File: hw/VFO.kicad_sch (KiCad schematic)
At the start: 0 parts

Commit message: Starting design of RF front end and demod
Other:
- title: USB SSB Transciever overview -> VF)
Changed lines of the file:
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@@
 	(paper "A")
 	(title_block
-		(title "USB SSB Transciever overview")
+		(title "VF)")
 		(date "2025-03-23")
 		(company "SoftShack")

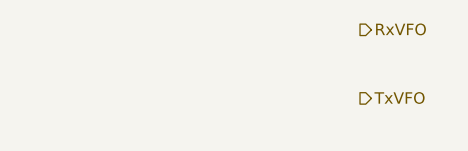
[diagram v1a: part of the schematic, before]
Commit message: Rx path is getting closer. Differential LO outputs from VFO. Clean up.
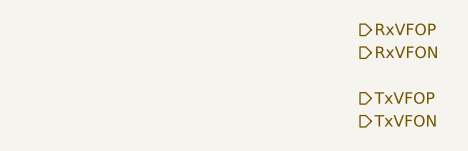
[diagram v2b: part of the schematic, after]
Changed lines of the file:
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@@
 		(comment 2 "WB7NAB")
 	)
-	(hierarchical_label "RxVFO"
+	(hierarchical_label "RxVFOP"
 		(shape output)
 		(at 256.54 25.4 0)
@@
 		)
 	)
-	(hierarchical_label "TxVFO"
+	(hierarchical_label "TxVFON"
+		(shape output)
+		(at 256.54 35.56 0)
+		(effects
+			(font
+				(size 1.27 1.27)
+			)
+			(justify left)
+		)
+	)
+	(hierarchical_label "TxVFOP"
 		(shape output)
 		(at 256.54 33.02 0)
@@
 		(effects
 			(font
+				(size 1.27 1.27)
+			)
+			(justify left)
+		)
+	)
+	(hierarchical_label "RxVFON"
+		(shape output)
+		(at 256.54 27.94 0)
+		(effects
+			(font

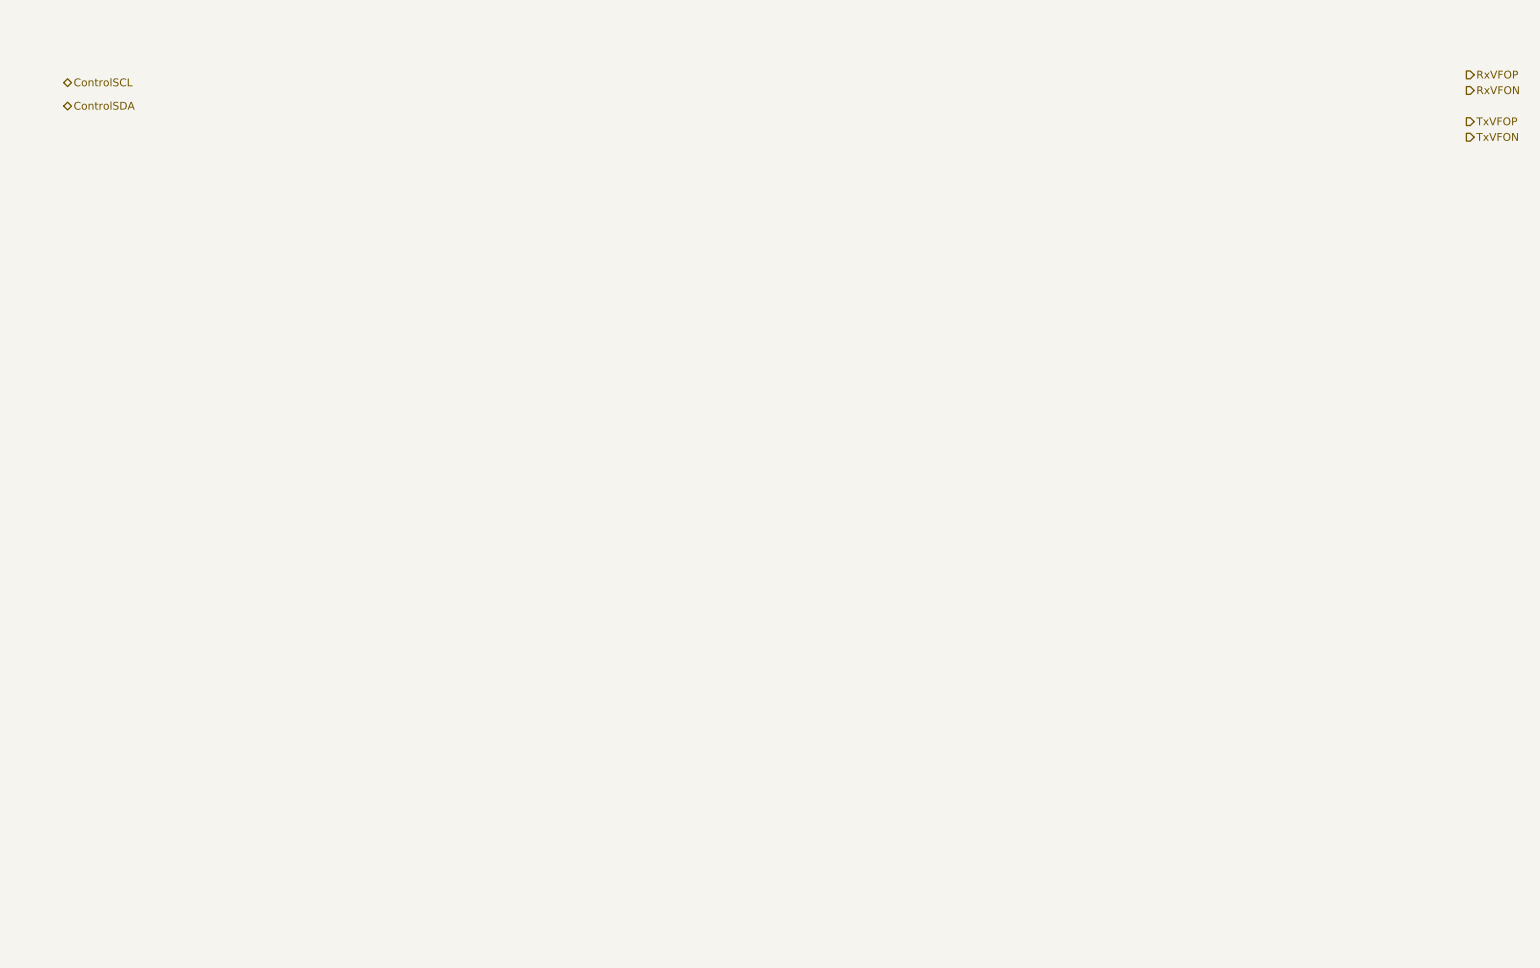
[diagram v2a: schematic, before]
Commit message: Checkpoint. More of rx path done. VFOs are now LVDS. Starting USB and power.
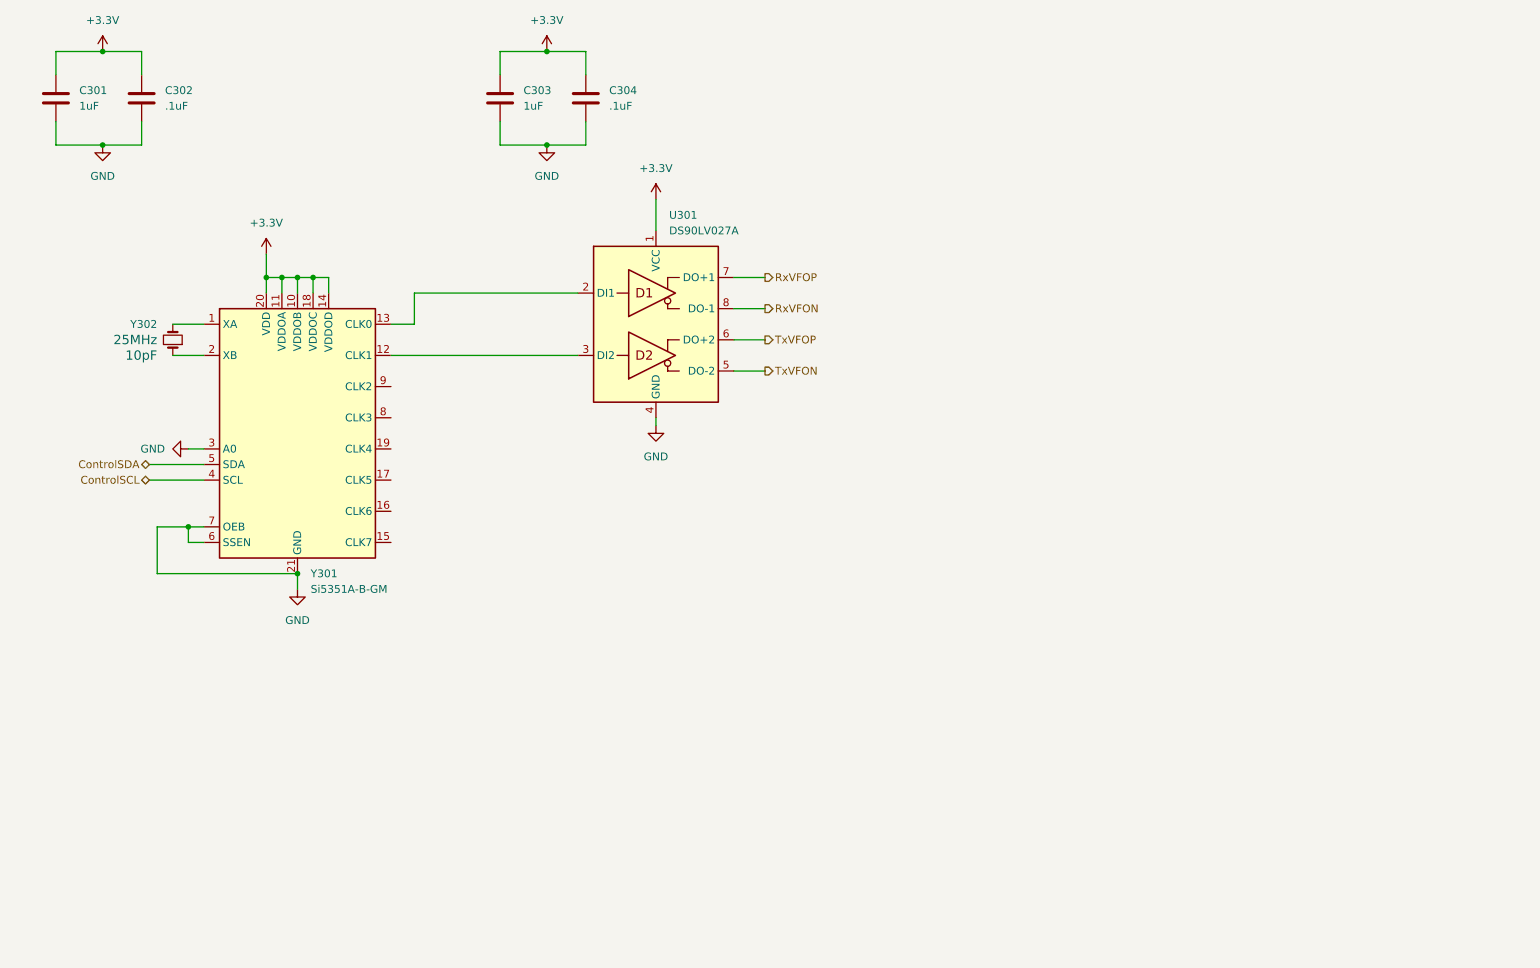
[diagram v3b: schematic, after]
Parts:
- added C301, C303: 1uF, symbol Device:C
- added C302, C304: .1uF, symbol Device:C
- added U301: DS90LV027A, Package_SO:SOIC-8_3.9x4.9mm_P1.27mm, symbol Interface:DS90LV027A
- added Y301: Si5351A-B-GM, Package_DFN_QFN:QFN-20-1EP_4x4mm_P0.5mm_EP2.7x2.7mm, symbol Oscillator:Si5351A-B-GM
- added Y302: 25MHz FA-238 25.0000MB-K, 4ms_Crystal:FA-238, symbol PCM_4ms_Crystal:16MHz_18pF_FA238
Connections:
- net ControlSCL: now also Y301.4 (SCL)
- net ControlSDA: now also Y301.5 (SDA)
- net RxVFON: now also U301.8 (DO-1)
- net RxVFOP: now also U301.7 (DO+1)
- net TxVFON: now also U301.5 (DO-2)
- net TxVFOP: now also U301.6 (DO+2)
- new net: Y301.1 (XA), Y302.2
- new net: U301.3 (DI2), Y301.12 (CLK1)
- new net: U301.2 (DI1), Y301.13 (CLK0)
- new net: Y301.2 (XB), Y302.1
- new net +3.3V: C301.2, C302.2, C303.2, C304.2, U301.1 (VCC), Y301.10 (VDDOB), Y301.11 (VDDOA), Y301.14 (VDDOD), Y301.18 (VDDOC), Y301.20 (VDD)
- new net GND: C301.1, C302.1, C303.1, C304.1, U301.4 (GND), Y301.21 (GND), Y301.3 (A0), Y301.6 (SSEN), Y301.7 (OEB)
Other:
- title: VF) -> VFO and clocks

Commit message: Restructure power and USB sheets a bit. Generate each power rail we need so far from USB VBUS, but still need to control VBUS input with TI USBPD chip. Set up USB2 data net class and power and GND netclasses.
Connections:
- no-connect marks 0 -> 6
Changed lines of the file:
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@@
 	(title_block
 		(title "VFO and clocks")
-		(date "2025-03-25")
+		(date "2025-03-26")
 		(company "SoftShack")
 		(comment 1 "Alan Mimms")
@@
 		(color 0 0 0 0)
 	)
+	(no_connect
+		(at 81.28 96.52)
+	)
+	(no_connect
+		(at 81.28 76.2)
+	)
+	(no_connect
+		(at 81.28 101.6)
+	)
+	(no_connect
+		(at 81.28 91.44)
+	)
+	(no_connect
+		(at 81.28 86.36)
+	)
+	(no_connect
+		(at 81.28 81.28)
+	)
 	(wire

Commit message: Checkpoint before resuming project
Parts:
- renumbered Y302 to Y301, Y301 to Y302
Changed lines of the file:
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@@
 		(dnp no)
 		(fields_autoplaced yes)
-		(property "Reference" "#PWR0308"
+		(property "Reference" "#PWR0307"
 			(at 106.68 43.18 0)
 			(effects
@@
 			(project "USB-SSB-txcvr"
 				(path "/8ae46c04-d01a-4756-8774-512b694bfaff/dab9d1f1-a255-4db5-bc55-08fa1f9f2738"
-					(reference "#PWR0308")
+					(reference "#PWR0307")
 					(unit 1)
 				)
@@
 		(dnp no)
 		(fields_autoplaced yes)
-		(property "Reference" "Y301"
+		(property "Reference" "Y302"
 			(at 68.1833 106.68 0)
 			(effects
@@
 			(project ""
 				(path "/8ae46c04-d01a-4756-8774-512b694bfaff/dab9d1f1-a255-4db5-bc55-08fa1f9f2738"
-					(reference "Y301")
+					(reference "Y302")
 					(unit 1)
 				)
@@
 		(dnp no)
 		(fields_autoplaced yes)
-		(property "Reference" "#PWR0301"
+		(property "Reference" "#PWR0303"
 			(at 41.91 86.36 0)
 			(effects
@@
 			(project ""
 				(path "/8ae46c04-d01a-4756-8774-512b694bfaff/dab9d1f1-a255-4db5-bc55-08fa1f9f2738"
-					(reference "#PWR0301")
+					(reference "#PWR0303")
 					(unit 1)
 				)
@@
 		(dnp no)
 		(fields_autoplaced yes)
-		(property "Reference" "#PWR0307"
+		(property "Reference" "#PWR0306"
 			(at 106.68 25.4 0)
 			(effects
@@
 			(project "USB-SSB-txcvr"
 				(path "/8ae46c04-d01a-4756-8774-512b694bfaff/dab9d1f1-a255-4db5-bc55-08fa1f9f2738"
-					(reference "#PWR0307")
+					(reference "#PWR0306")
 					(unit 1)
 				)
@@
 		(dnp no)
 		(fields_autoplaced yes)
-		(property "Reference" "#PWR0304"
+		(property "Reference" "#PWR0308"
 			(at 124.46 49.53 0)
 			(effects
@@
 			(project "USB-SSB-txcvr"
 				(path "/8ae46c04-d01a-4756-8774-512b694bfaff/dab9d1f1-a255-4db5-bc55-08fa1f9f2738"
-					(reference "#PWR0304")
+					(reference "#PWR0308")
 					(unit 1)
 				)
@@
 		(on_board yes)
 		(dnp no)
-		(property "Reference" "Y302"
+		(property "Reference" "Y301"
 			(at 43.18 66.0399 90)
 			(effects
@@
 			(project ""
 				(path "/8ae46c04-d01a-4756-8774-512b694bfaff/dab9d1f1-a255-4db5-bc55-08fa1f9f2738"
-					(reference "Y302")
+					(reference "Y301")
 					(unit 1)
 				)
@@
 		(dnp no)
 		(fields_autoplaced yes)
-		(property "Reference" "#PWR0302"
+		(property "Reference" "#PWR0305"
 			(at 66.04 115.57 0)
 			(effects
@@
 			(project "USB-SSB-txcvr"
 				(path "/8ae46c04-d01a-4756-8774-512b694bfaff/dab9d1f1-a255-4db5-bc55-08fa1f9f2738"
-					(reference "#PWR0302")
+					(reference "#PWR0305")
 					(unit 1)
 				)
@@
 		(dnp no)
 		(fields_autoplaced yes)
-		(property "Reference" "#PWR0305"
+		(property "Reference" "#PWR0302"
 			(at 34.29 43.18 0)
 			(effects
@@
 			(project "USB-SSB-txcvr"
 				(path "/8ae46c04-d01a-4756-8774-512b694bfaff/dab9d1f1-a255-4db5-bc55-08fa1f9f2738"
-					(reference "#PWR0305")
+					(reference "#PWR0302")
 					(unit 1)
 				)
@@
 		(dnp no)
 		(fields_autoplaced yes)
-		(property "Reference" "#PWR0306"
+		(property "Reference" "#PWR0301"
 			(at 34.29 25.4 0)
 			(effects
@@
 			(project "USB-SSB-txcvr"
 				(path "/8ae46c04-d01a-4756-8774-512b694bfaff/dab9d1f1-a255-4db5-bc55-08fa1f9f2738"
-					(reference "#PWR0306")
+					(reference "#PWR0301")
 					(unit 1)
 				)
@@
 		(dnp no)
 		(fields_autoplaced yes)
-		(property "Reference" "#PWR0303"
+		(property "Reference" "#PWR0304"
 			(at 60.96 58.42 0)
 			(effects
@@
 			(project ""
 				(path "/8ae46c04-d01a-4756-8774-512b694bfaff/dab9d1f1-a255-4db5-bc55-08fa1f9f2738"
-					(reference "#PWR0303")
-					(unit 1)
-				)
+					(reference "#PWR0304")
+					(unit 1)
+				)

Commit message: Working on multi-band BPF and switching
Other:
- company: SoftShack -> WB7NAB
- title: VFO and clocks -> ${title}
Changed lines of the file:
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@@
 	(generator "eeschema")
 	(generator_version "9.0")
-	(paper "A")
+	(paper "USLetter")
 	(title_block
-		(title "VFO and clocks")
-		(date "2025-03-26")
-		(company "SoftShack")
+		(title "${title}")
+		(date "2025-08-10")
+		(company "WB7NAB")
 		(comment 1 "Alan Mimms")
-		(comment 2 "WB7NAB")
 	)
 	(junction

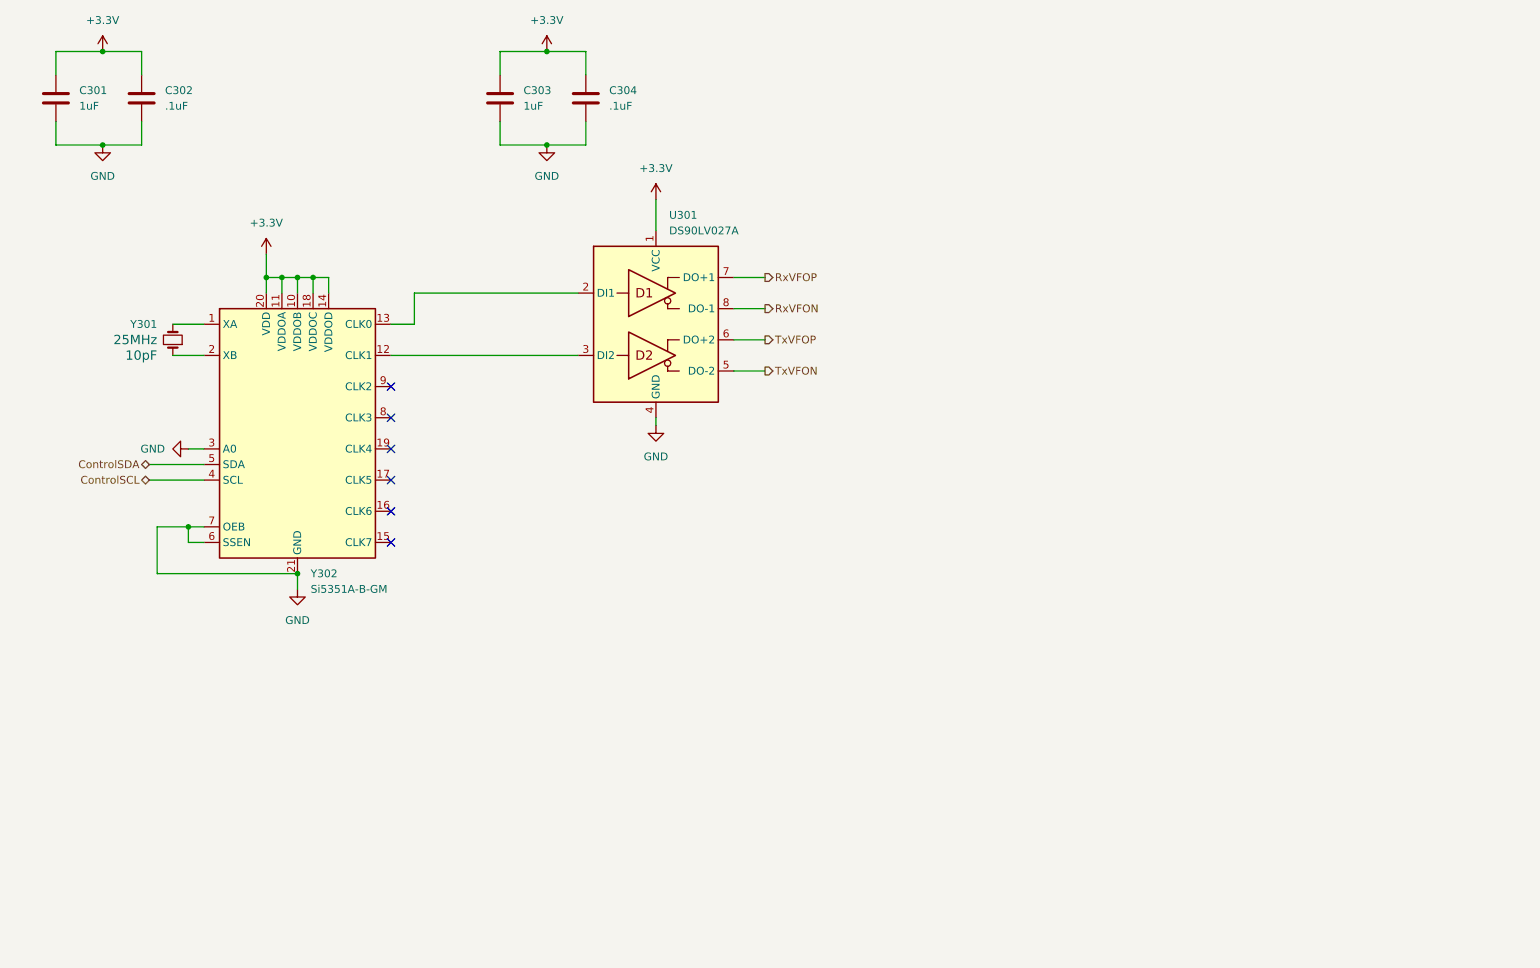
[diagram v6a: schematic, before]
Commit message: Starting to build BPFs for 7 bands
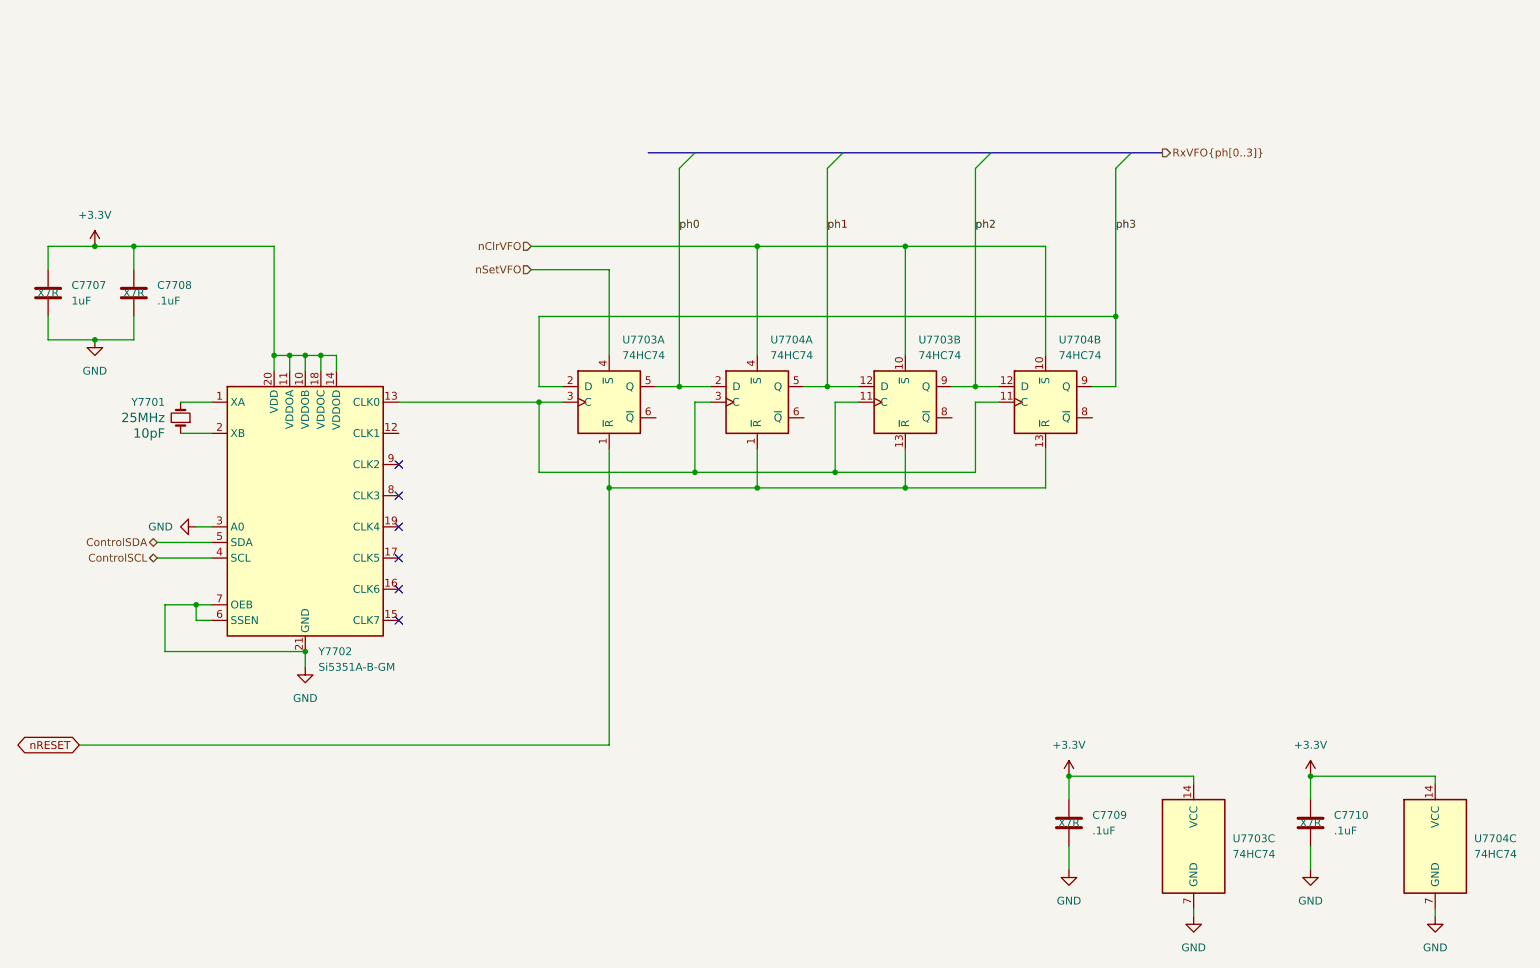
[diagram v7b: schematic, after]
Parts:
- removed C303: 1uF, symbol Device:C
- removed U301: DS90LV027A, Package_SO:SOIC-8_3.9x4.9mm_P1.27mm, symbol Interface:DS90LV027A
- added C7710: .1uF, symbol Device:C
- added U7703, U7704: 74HC74, symbol 74xx:74HC74
- C7707: renamed from C301; cap-type (none) -> X7R
- C7708: renamed from C302; cap-type (none) -> X7R
- C7709: renamed from C304; cap-type (none) -> X7R
- renumbered Y301 to Y7701, Y302 to Y7702
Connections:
- net +3.3V: now also C7710.2, U7703.14 (VCC), U7704.14 (VCC)
- net GND: now also C7710.1, U7703.7 (GND), U7704.7 (GND)
- net at Y7702.13 (CLK0): now also U7703.11 (C), U7703.3 (C), U7704.11 (C), U7704.3 (C)
- new net nClrVFO: U7703.10 (~{S}), U7704.10 (~{S}), U7704.4 (~{S})
- new net nRESET: U7703.1 (~{R}), U7703.13 (~{R}), U7704.1 (~{R}), U7704.13 (~{R})
- new net nSetVFO: U7703.4 (~{S})
- new net ph0: U7703.5 (Q), U7704.2 (D)
- new net ph1: U7703.12 (D), U7704.5 (Q)
- new net ph2: U7703.9 (Q), U7704.12 (D)
- new net ph3: U7703.2 (D), U7704.9 (Q)
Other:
- title: ${title} -> VFO and Clocks
- moved on the sheet: C7707, C7708, C7709, Y7701, Y7702
